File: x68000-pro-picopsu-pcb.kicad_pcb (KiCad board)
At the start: 2 copper layers, 209 x 98 mm, 27 parts, among them J1 Fan Header, J2 Screw_Terminal_01x07, J3 Screw_Terminal_01x07, J4 PicoPSU, U1 74LS04

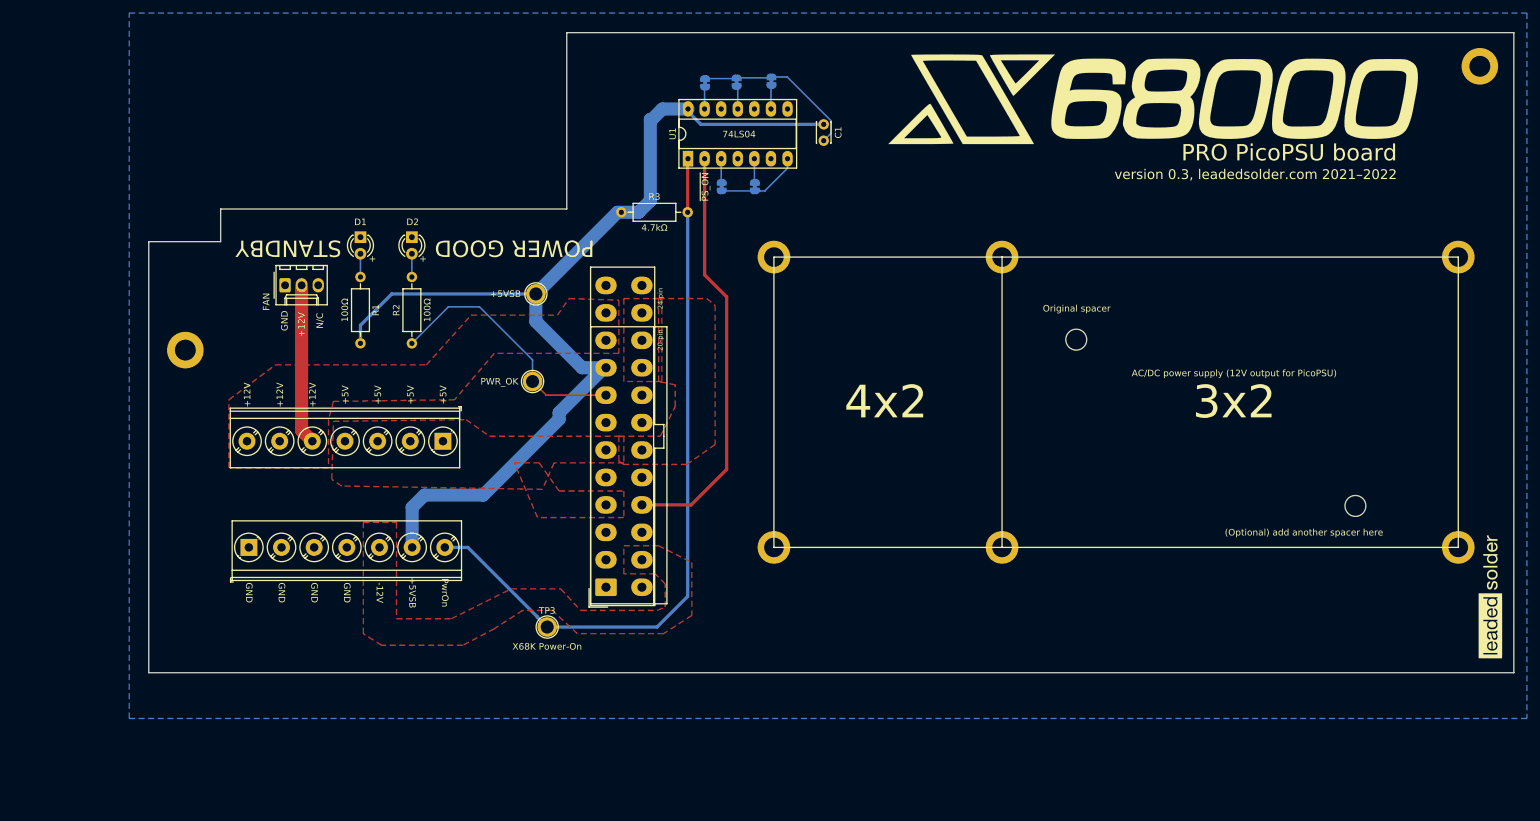
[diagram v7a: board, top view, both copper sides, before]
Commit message: Add protection resistor to power-on signal to protect syscon just in case
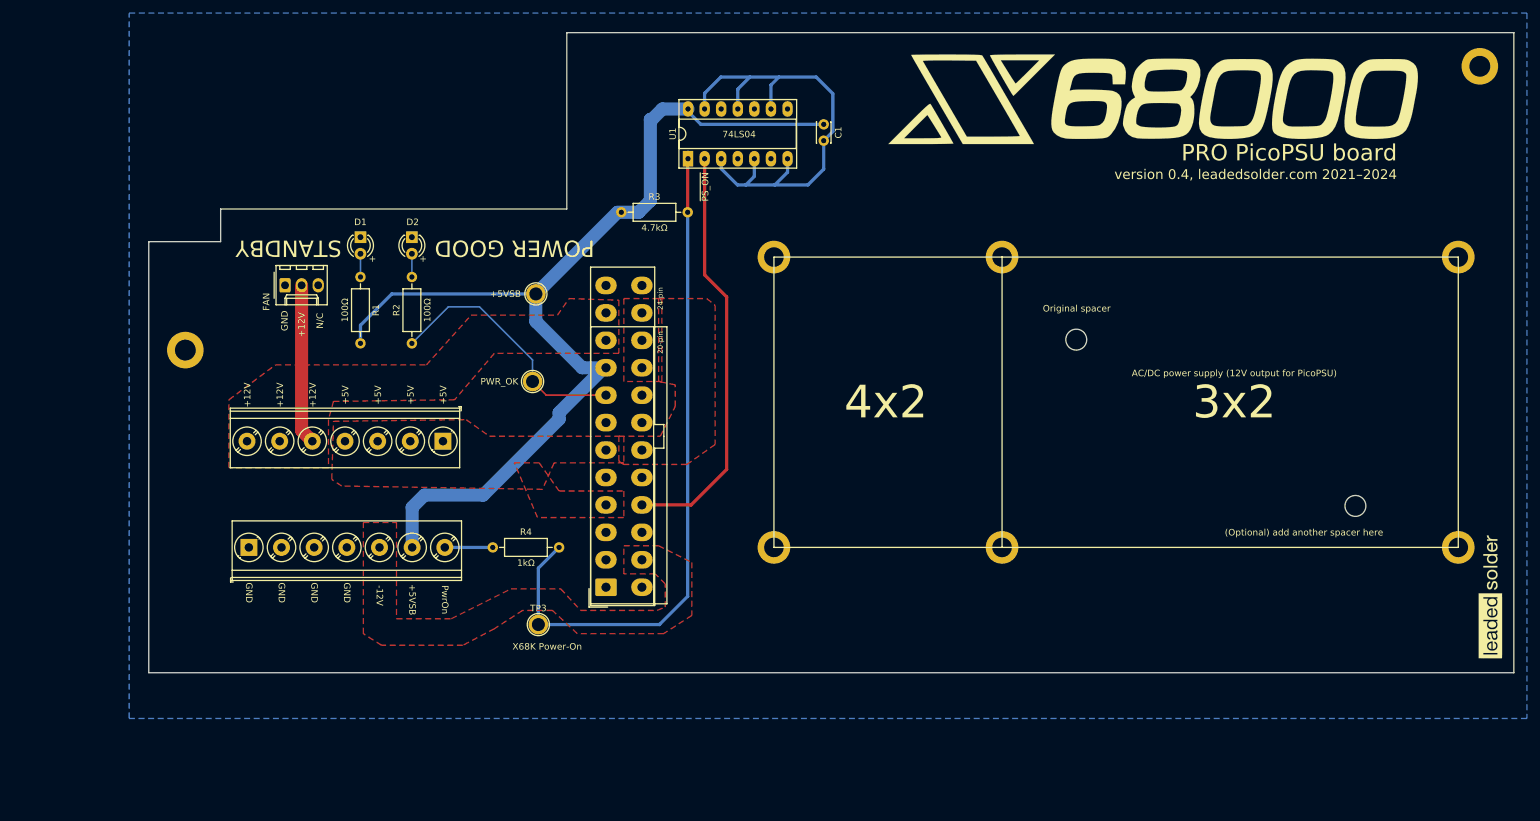
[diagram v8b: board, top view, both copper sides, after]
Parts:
- removed JP1, JP2, JP3, JP4, JP5: N/C, Jumper:SolderJumper-2_P1.3mm_Bridged_RoundedPad1.0x1.5mm
- added R4: 1kΩ, Resistor_THT:R_Axial_DIN0207_L6.3mm_D2.5mm_P10.16mm_Horizontal, F.Cu at (91.4, 117.1)
- moved TP3 1.41 mm to (98.4, 128.9)
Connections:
- net /~PS_ON renamed /~{PS_ON}
- J1 pad 3: Net-(J1-Pad3) -> unconnected-(J1-Pin_3-Pad3)
- J3 pad 7: /POWER_ON_REQUEST -> Net-(J3-Pin_7)
- J4 pad 1: Net-(J4-Pad1) -> unconnected-(J4-+3.3V-Pad1)
- J4 pad 12: Net-(J4-Pad12) -> unconnected-(J4-+3.3V-Pad12)
- J4 pad 13: Net-(J4-Pad13) -> unconnected-(J4-+3.3V-Pad13)
- J4 pad 2: Net-(J4-Pad2) -> unconnected-(J4-+3.3V-Pad2)
- J4 pad 20: Net-(J4-Pad20) -> unconnected-(J4--5V?-Pad20)
- U1 pad 10: Net-(U1-Pad10) -> unconnected-(U1-Pad10)
- U1 pad 11: Net-(JP4-Pad2) -> /PSU_COM
- U1 pad 12: Net-(U1-Pad12) -> unconnected-(U1-Pad12)
- U1 pad 13: Net-(JP5-Pad2) -> /PSU_COM
- U1 pad 3: Net-(JP1-Pad2) -> /PSU_COM
- U1 pad 4: Net-(U1-Pad4) -> unconnected-(U1-Pad4)
- U1 pad 5: Net-(JP2-Pad2) -> /PSU_COM
- U1 pad 6: Net-(U1-Pad6) -> unconnected-(U1-Pad6)
- U1 pad 8: Net-(U1-Pad8) -> unconnected-(U1-Pad8)
- U1 pad 9: Net-(JP3-Pad2) -> /PSU_COM
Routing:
- net /PSU_COM: track 38.7 -> 77.5 mm
- net Net-(J3-Pin_7): track 0.00 -> 7.34 mm
- net /POWER_ON_REQUEST: track 112.4 -> 105.9 mm
- net Net-(JP1-Pad2): track 3.66 -> 0.00 mm
- net Net-(JP2-Pad2): track 3.66 -> 0.00 mm
- net Net-(JP3-Pad2): track 3.63 -> 0.00 mm
- net Net-(JP4-Pad2): track 3.53 -> 0.00 mm
- net Net-(JP5-Pad2): track 3.37 -> 0.00 mm
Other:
- net class Default removed
- board text added: "version 0.4, leadedsolder.com 2021–2024"
- board text added: "~{PS_ON}"
- board text removed: "version 0.3, leadedsolder.com 2021–2022"
- board text removed: "~PS_ON"
